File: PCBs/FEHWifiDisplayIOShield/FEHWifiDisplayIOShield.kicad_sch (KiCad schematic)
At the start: 18 parts, among them J1 Conn_01x16_Socket, J2 Conn_02x04_Counter_Clockwise, J3 JST_2MM_MALE, SW1 SW_MEC_5G, SW2 SW_MEC_5G, SW3 SW_MEC_5G, SW4 SW_MEC_5G

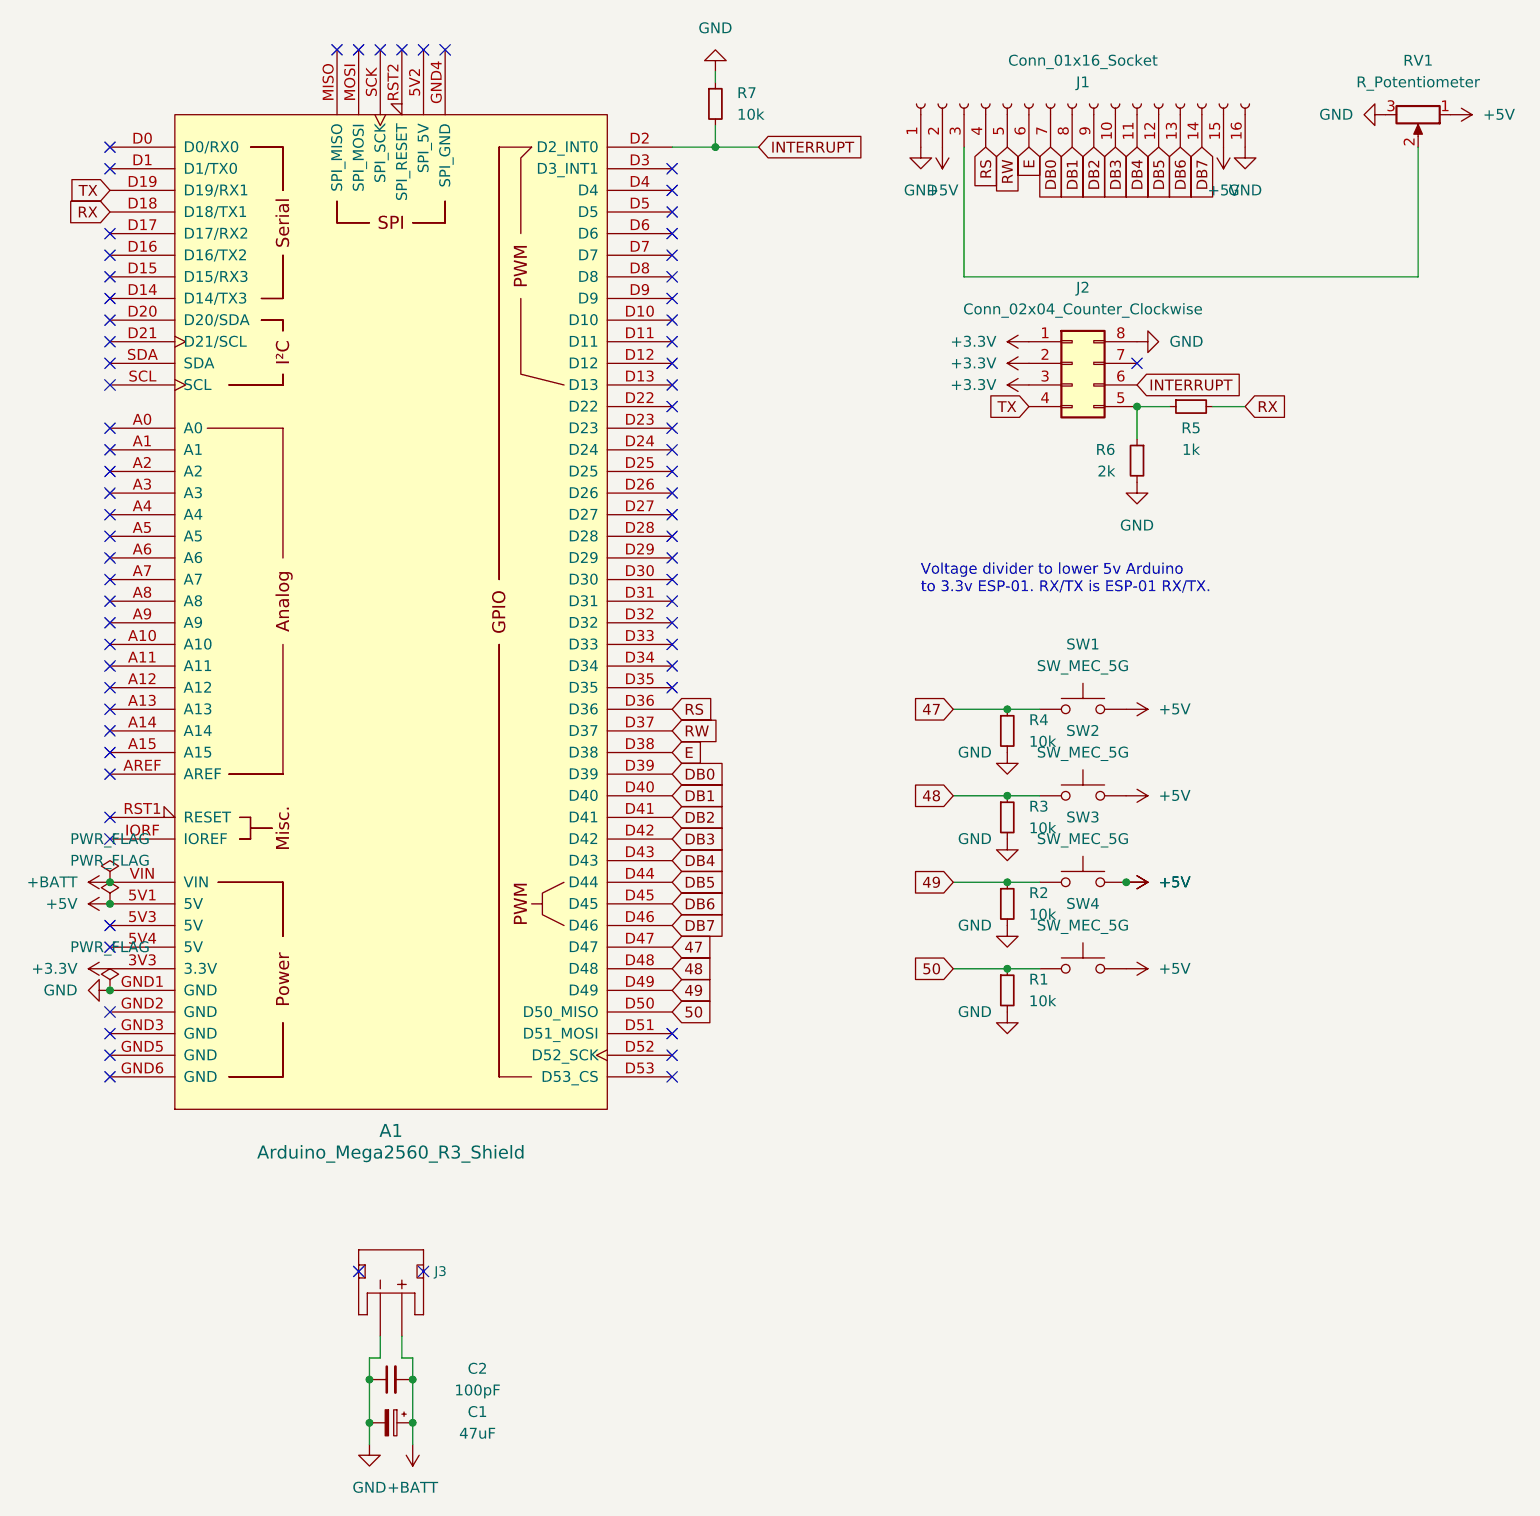
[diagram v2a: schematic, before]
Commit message: Configured LCD for 4 bit operation
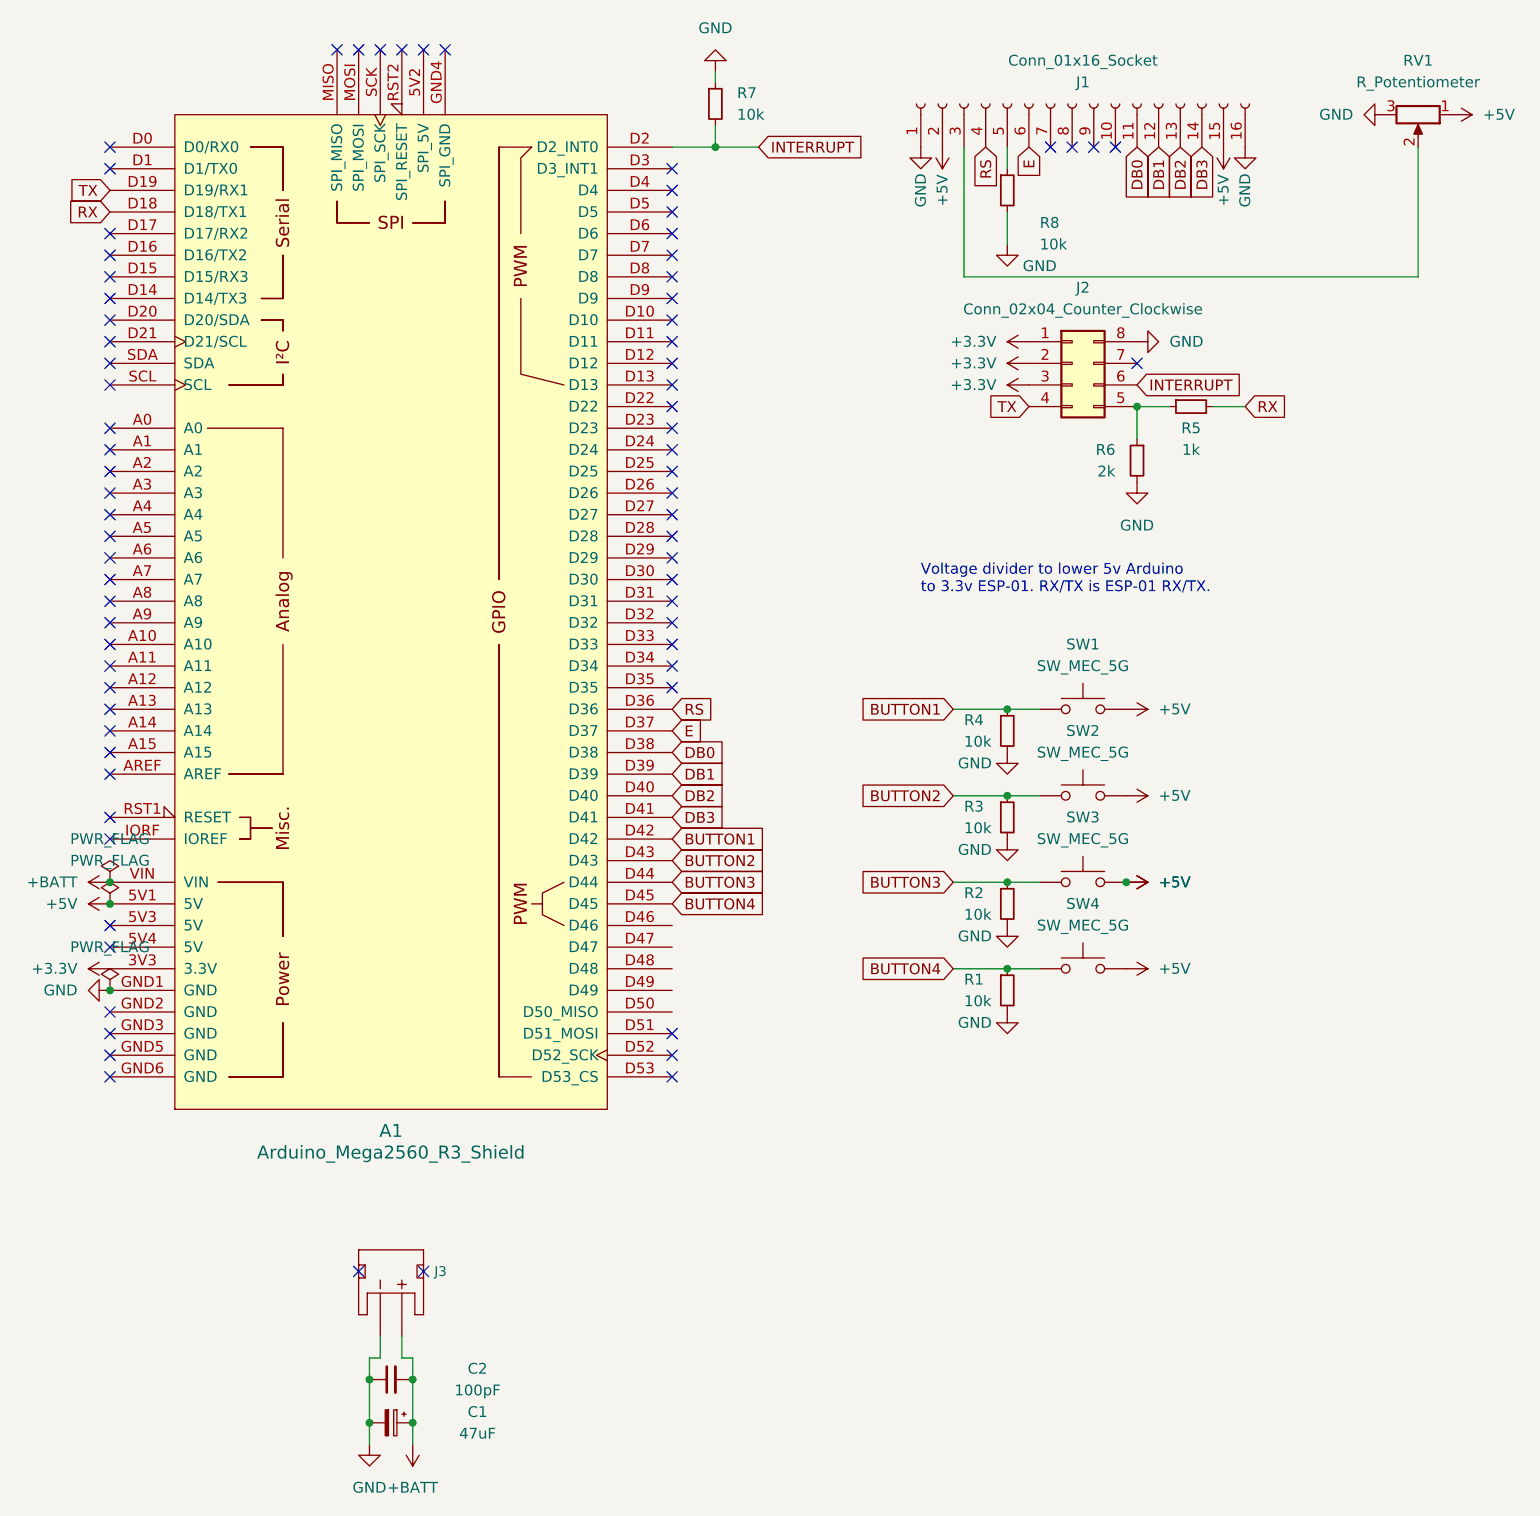
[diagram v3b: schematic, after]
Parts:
- added R8: 10k, symbol Device:R_Small
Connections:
- net DB0: now also A1.D38, J1.11 (Pin_11); no longer A1.D39, J1.7 (Pin_7)
- net DB1: now also A1.D39, J1.12 (Pin_12); no longer A1.D40, J1.8 (Pin_8)
- net DB2: now also A1.D40, J1.13 (Pin_13); no longer A1.D41, J1.9 (Pin_9)
- net DB3: now also A1.D41, J1.14 (Pin_14); no longer A1.D42, J1.10 (Pin_10)
- net E: now also A1.D37; no longer A1.D38
- net GND: now also R8.2
- net 47 renamed BUTTON1
- net BUTTON1: now also A1.D42; no longer A1.D47
- net 48 renamed BUTTON2
- net BUTTON2: now also A1.D43; no longer A1.D48
- net 49 renamed BUTTON3
- net BUTTON3: now also A1.D44; no longer A1.D49
- net 50 renamed BUTTON4
- net BUTTON4: now also A1.D45; no longer A1.D50 (D50_MISO)
- removed net DB4: A1.D43, J1.11 (Pin_11)
- removed net DB5: A1.D44, J1.12 (Pin_12)
- removed net DB6: A1.D45, J1.13 (Pin_13)
- net DB7: no longer names the net of A1.D46
- net DB7: no longer J1.14 (Pin_14)
- net RW: no longer names the net of J1.5 (Pin_5)
- net RW: now also R8.1; no longer A1.D37
- no-connect marks 72 -> 76
